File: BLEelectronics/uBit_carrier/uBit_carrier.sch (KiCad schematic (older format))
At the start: 7 parts, among them J1 microbit_edge_connector, J2 Conn_01x02_Male, U1 W25Q32JVSS, U2 XC6206PxxxMR

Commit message: Add tweaks to schematic with LCSC parts
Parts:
- C1: LCSC (none) -> C14663; MPN (none) -> CC0603KRX7R9BB104
- C2, C3: LCSC (none) -> C15849; MPN (none) -> CL10A105KB8NNNC
- U1: value W25Q32JVSS -> W25Q128JV; LCSC (none) -> C97521
- U2: value XC6206PxxxMR -> XC6206P332MR; LCSC (none) -> C5446
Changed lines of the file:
@@
 P 6900 3300
 F 0 "U1" H 6900 3881 50  0000 C CNN
-F 1 "W25Q32JVSS" H 6900 3790 50  0000 C CNN
+F 1 "W25Q128JV" H 6900 3790 50  0000 C CNN
 F 2 "Package_SO:SOIC-8_5.23x5.23mm_P1.27mm" H 6900 3300 50  0001 C CNN
 F 3 "http://www.winbond.com/resource-files/w25q32jv%20revg%2003272018%20plus.pdf" H 6900 3300 50  0001 C CNN
+F 4 "C97521" H 6900 3300 50  0001 C CNN "LCSC"
 	1    6900 3300
 	1    0    0    -1
@@
 F 2 "Capacitor_SMD:C_0603_1608Metric_Pad1.05x0.95mm_HandSolder" H 6938 2200 50  0001 C CNN
 F 3 "~" H 6900 2350 50  0001 C CNN
+F 4 "CC0603KRX7R9BB104" H 6900 2350 50  0001 C CNN "MPN"
+F 5 "C14663" H 6900 2350 50  0001 C CNN "LCSC"
 	1    6900 2350
 	1    0    0    -1
@@
 P 7900 2500
 F 0 "U2" H 7900 2649 50  0000 C CNN
-F 1 "XC6206PxxxMR" H 7900 2740 50  0000 C CNN
+F 1 "XC6206P332MR" H 7900 2740 50  0000 C CNN
 F 2 "Package_TO_SOT_SMD:SOT-23" H 7900 2725 50  0001 C CIN
 F 3 "https://www.torexsemi.com/file/xc6206/XC6206.pdf" H 7900 2500 50  0001 C CNN
+F 4 "C5446" H 7900 2500 50  0001 C CNN "LCSC"
 	1    7900 2500
 	-1   0    0    1
@@
 F 2 "Capacitor_SMD:C_0603_1608Metric_Pad1.05x0.95mm_HandSolder" H 7488 2200 50  0001 C CNN
 F 3 "~" H 7450 2350 50  0001 C CNN
+F 4 "CL10A105KB8NNNC" H 7450 2350 50  0001 C CNN "MPN"
+F 5 "C15849" H 7450 2350 50  0001 C CNN "LCSC"
 	1    7450 2350
 	1    0    0    -1
@@
 Wire Wire Line
 	7450 1700 7900 1700
-$Comp
-L Device:C C3
-U 1 1 5EC74158
-P 8350 2300
-F 0 "C3" H 8465 2346 50  0000 L CNN
-F 1 "1uF" H 8465 2255 50  0000 L CNN
-F 2 "Capacitor_SMD:C_0603_1608Metric_Pad1.05x0.95mm_HandSolder" H 8388 2150 50  0001 C CNN
-F 3 "~" H 8350 2300 50  0001 C CNN
-	1    8350 2300
-	1    0    0    -1
-$EndComp
 Wire Wire Line
 	8200 2500 8350 2500
@@
 Text Label 5800 3900 0    50   ~ 0
 ~CS
+$Comp
+L Device:C C3
+U 1 1 5ECA190C
+P 8350 2300
+F 0 "C3" H 8465 2346 50  0000 L CNN
+F 1 "1uF" H 8465 2255 50  0000 L CNN
+F 2 "Capacitor_SMD:C_0603_1608Metric_Pad1.05x0.95mm_HandSolder" H 8388 2150 50  0001 C CNN
+F 3 "~" H 8350 2300 50  0001 C CNN
+F 4 "CL10A105KB8NNNC" H 8350 2300 50  0001 C CNN "MPN"
+F 5 "C15849" H 8350 2300 50  0001 C CNN "LCSC"
+	1    8350 2300
+	1    0    0    -1
+$EndComp
 $EndSCHEMATC

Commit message: Progress as of 3:30 PM MDT... Passing off to Matt
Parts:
- added J3: Micro_SD_Card_Det_Hirose_DM3AT, Connector_Card:microSD_HC_Hirose_DM3AT-SF-PEJM5, symbol Connector:Micro_SD_Card_Det_Hirose_DM3AT
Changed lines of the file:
@@
+	1    0    0    -1
+$EndComp
+$Comp
+L Connector:Micro_SD_Card_Det_Hirose_DM3AT J3
+U 1 1 5ECA2AC0
+P 8900 4650
+F 0 "J3" H 8850 5467 50  0000 C CNN
+F 1 "Micro_SD_Card_Det_Hirose_DM3AT" H 8850 5376 50  0000 C CNN
+F 2 "Connector_Card:microSD_HC_Hirose_DM3AT-SF-PEJM5" H 10950 5350 50  0001 C CNN
+F 3 "https://www.hirose.com/product/en/download_file/key_name/DM3/category/Catalog/doc_file_id/49662/?file_category_id=4&item_id=195&is_series=1" H 8900 4750 50  0001 C CNN
+	1    8900 4650
 	1    0    0    -1
 $EndComp

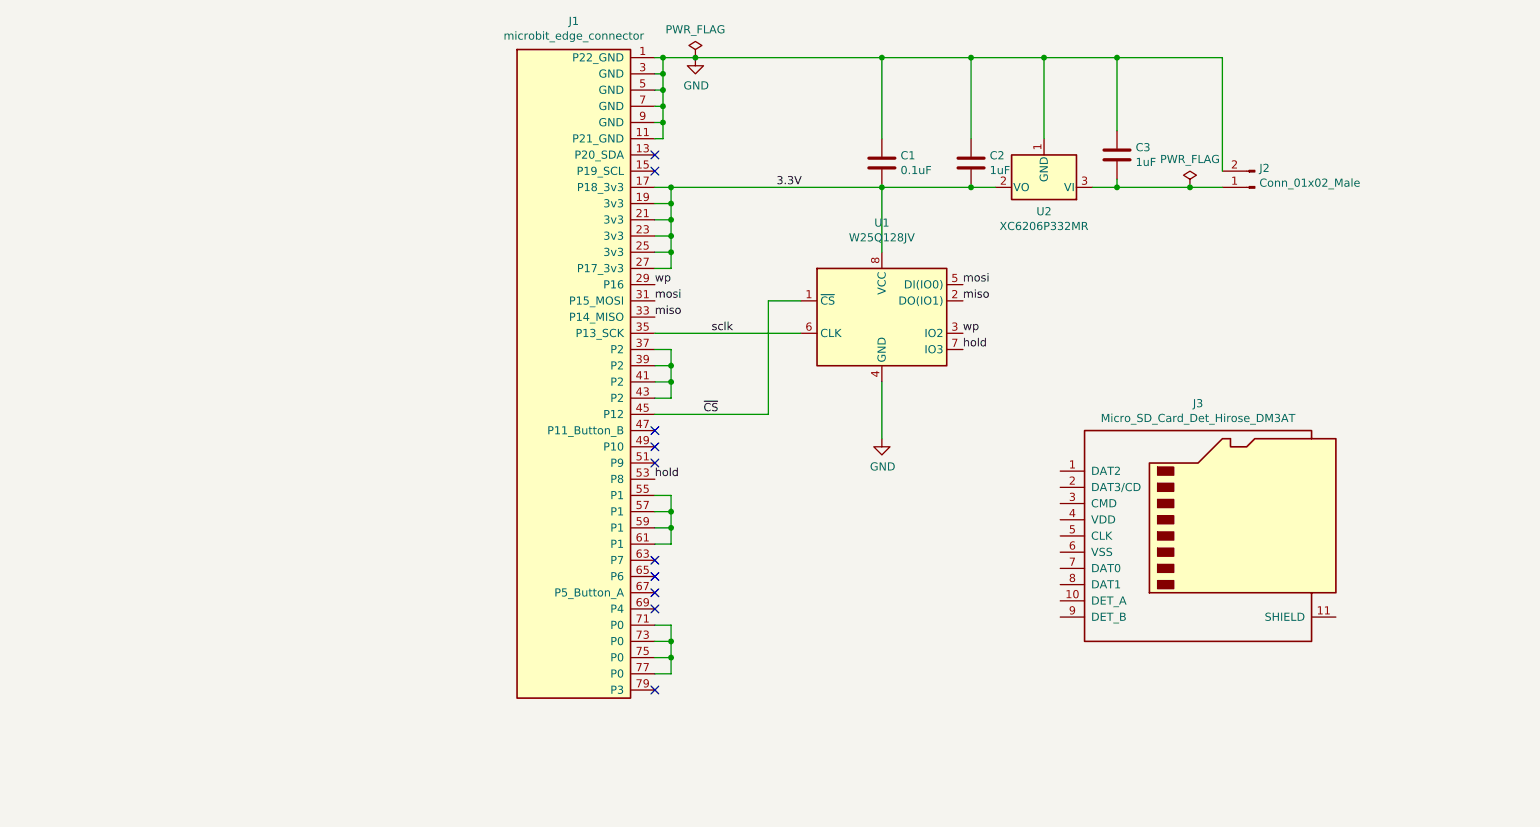
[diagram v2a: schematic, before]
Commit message: Full sch and layout of uBit carrier.
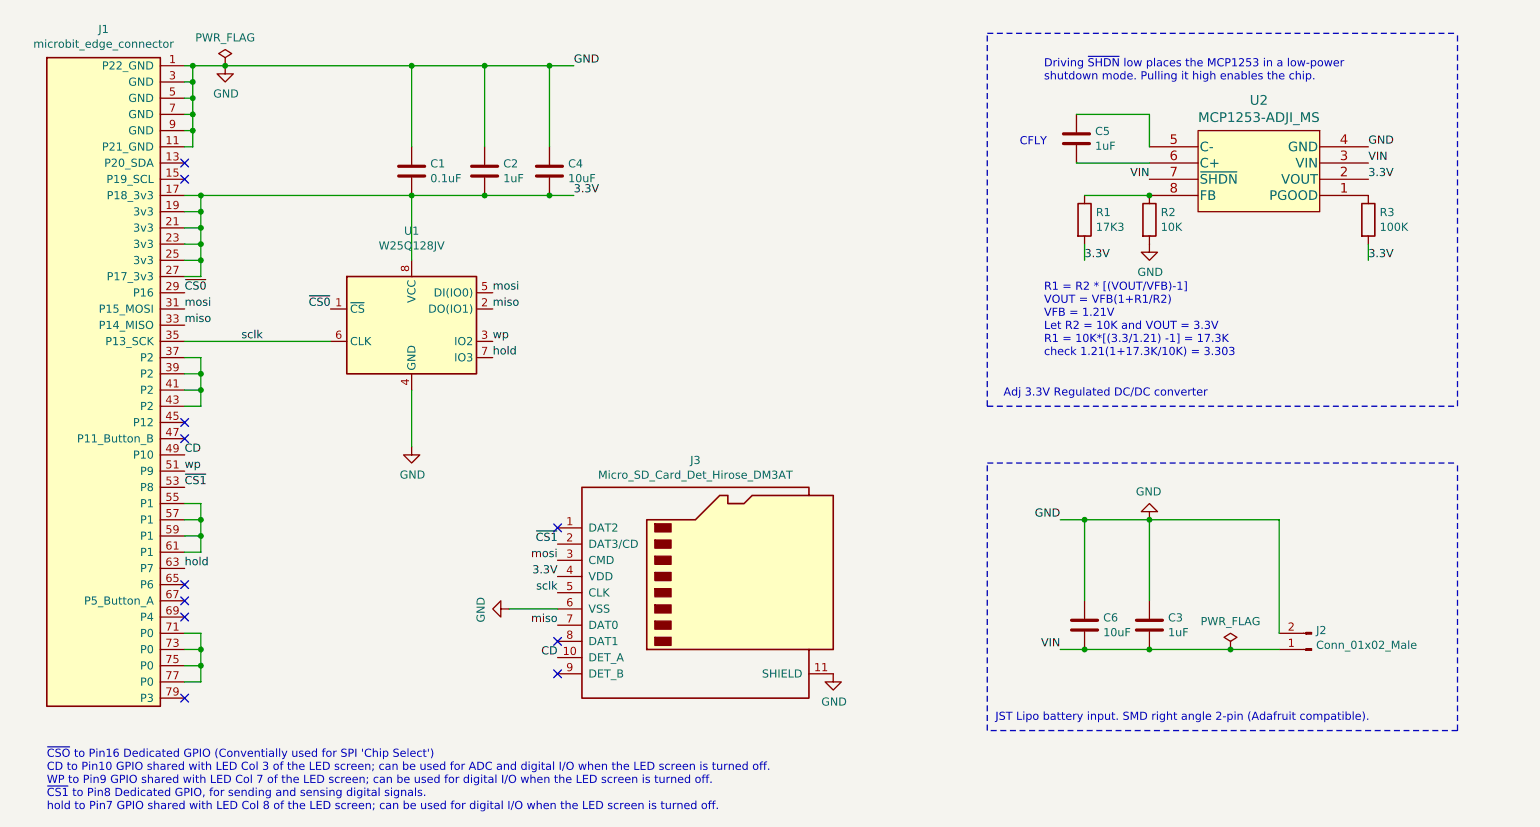
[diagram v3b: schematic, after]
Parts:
- removed U2: XC6206P332MR, Package_TO_SOT_SMD:SOT-23, symbol Regulator_Linear:XC6206PxxxMR
- added C4, C6: 10uF, Capacitor_SMD:C_0603_1608Metric, symbol Device:C
- added C5: 1uF, Capacitor_SMD:C_0603_1608Metric_Pad1.05x0.95mm_HandSolder, symbol Device:C
- added R1: 17K3, Resistor_SMD:R_0603_1608Metric, symbol Device:R
- added R2: 10K, Resistor_SMD:R_0603_1608Metric, symbol Device:R
- added R3: 100K, Resistor_SMD:R_0603_1608Metric, symbol Device:R
- added U2: MCP1253-ADJI_MS, 0my_footprints:MCP1253-ADJI_MS, symbol MCP1253-ADJI_MS:MCP1253-ADJI_MS
- J2: DPN (none) -> 455-1749-1-ND; LCSCPN (none) -> C295747; MFR (none) -> JST Sales America Inc.; MPN (none) -> S2B-PH-SM4-TB(LF)(SN)
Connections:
- net 3.3V: now also J3.4 (VDD), C4.2, R1.2, R3.2, U2.2 (VOUT)
- net GND: now also J3.11 (SHIELD), J3.6 (VSS), C4.1, C6.1, R2.2, U2.4 (GND)
- net hold: now also J1.63 (P7); no longer J1.53 (P8)
- net miso: now also J3.7 (DAT0)
- net mosi: now also J3.3 (CMD)
- net sclk: now also J3.5 (CLK)
- net wp: now also J1.51 (P9); no longer J1.29 (P16)
- net CD: now reaches J1.49 (P10)
- net CD: now also J3.10 (DET_A)
- net VIN: now reaches C3.2, J2.1 (Pin_1)
- net VIN: now also C6.2, U2.3 (VIN), U2.7 (~SHDN~)
- net ~CS1: now reaches J3.2 (DAT3/CD)
- net ~CS1: now also J1.53 (P8)
- net ~CS: no longer names the net of J1.45 (P12)
- net ~CS: no longer U1.1 (~CS)
- new net: C5.1, U2.5 (C-)
- new net: C5.2, U2.6 (C+)
- new net: R3.1, U2.1 (PGOOD)
- new net: R1.1, R2.1, U2.8 (FB)
- new net ~CS0: J1.29 (P16), U1.1 (~CS)
- no-connect marks 10 -> 11
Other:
- note added: "Adj 3.3V Regulated DC/DC converter"
- note added: "CFLY"
- note added: "Driving ~SHDN~ low places the MCP1253 in a low-power \nshutdown mode. Pulling it high enables the chip."
- note added: "JST Lipo battery input. SMD right angle 2-pin (Adafruit compatible)."
- note added: "R1 = R2 * [(VOUT/VFB)-1]\nVOUT = VFB(1+R1/R2)\nVFB = 1.21V\nLet R2 = 10K and VOUT = 3.3V\nR1 = 10K*[(3.3/1.21) -1] = 17.3K\ncheck 1.21(1+17.3K/10K) = 3.303\n"
- note added: "~CSO~ to Pin16 Dedicated GPIO (Conventially used for SPI 'Chip Select')\nCD to Pin10 GPIO shared with LED Col 3 of the LED screen; can be used for ADC and digital I/O when the LED screen is turned off.\nWP to Pin9 GPIO shared with LED Col 7 of the LED screen; can be used for digital I/O when the LED screen is turned off.\n~CS1~ to Pin8 Dedicated GPIO, for sending and sensing digital signals.\nhol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"
- moved on the sheet: C1, C2, C3, J1, J2, J3, U1

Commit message: uBit carrier BOM clean, gerbers DRC clean.
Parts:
- C1: value 0.1uF -> 100nF; footprint Capacitor_SMD:C_0603_1608Metric_Pad1.05x0.95mm_HandSolder -> Capacitor_SMD:C_0603_1608Metric; DPN (none) -> 311-1344-2-ND; LCSCPN (none) -> C14663; MFR (none) -> Yageo; SIM (none) -> -; SPN (none) -> -; SPR (none) -> -
- C2, C3, C5: footprint Capacitor_SMD:C_0603_1608Metric_Pad1.05x0.95mm_HandSolder -> Capacitor_SMD:C_0603_1608Metric; DPN (none) -> 445-1416-1-ND; LCSCPN (none) -> C385893; MFR (none) -> TDK Corporation; MPN CL10A105KB8NNNC -> C1608X5R1C105K080AA; SIM (none) -> -; SPN (none) -> -; SPR (none) -> -
- C4, C6: footprint Capacitor_SMD:C_0603_1608Metric -> Capacitor_SMD:C_0805_2012Metric; DPN (none) -> -; LCSCPN (none) -> C126586; MFR (none) -> Murata; MPN (none) -> GCM21BR71A106KE22L; SIM (none) -> -; SPN (none) -> -; SPR (none) -> -
- J1: DPN (none) -> -; LCSCPN (none) -> -; MFR (none) -> -; MPN (none) -> -; SIM (none) -> -; SPN (none) -> -; SPR (none) -> -
- J2: SIM (none) -> -; SPN (none) -> -; SPR (none) -> -
- J3: DPN (none) -> HR1964CT-ND; LCSCPN (none) -> C114218; MFR (none) -> Hirose; MPN (none) -> DM3AT-SF-PEJM5; SIM (none) -> -; SPN (none) -> -; SPR (none) -> -
- R1: value 17K3 -> 17K4; DPN (none) -> -; LCSCPN (none) -> C234322; MFR (none) -> Viking Tech; MPN (none) -> AR03FTC1742; SIM (none) -> -; SPN (none) -> -; SPR (none) -> -
- R2: DPN (none) -> 311-10KGRCT-ND; LCSCPN (none) -> C209220; MFR (none) -> Yageo; MPN (none) -> RC0603JR-0710KL; SIM (none) -> RMS06JT103; SPN (none) -> -; SPR (none) -> -
- R3: DPN (none) -> -; LCSCPN (none) -> C269682; MFR (none) -> TyoHM; MPN (none) -> RMC0603100K5%N; SIM (none) -> -; SPN (none) -> -; SPR (none) -> -
- U1: LCSCPN (none) -> C113767; MFR (none) -> Wirbond Elec; MPN (none) -> W25Q128JVSIQ; SIM (none) -> -; SPN (none) -> -; SPR (none) -> -
- U2: DPN (none) -> MCP1253-ADJI/MS-ND; LCSCPN (none) -> C144295; MFR (none) -> Microchip Tech; MPN (none) -> MCP1253-ADJI/MS; SIM (none) -> -; SPN (none) -> -; SPR (none) -> -
